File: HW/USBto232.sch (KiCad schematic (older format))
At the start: 14 parts

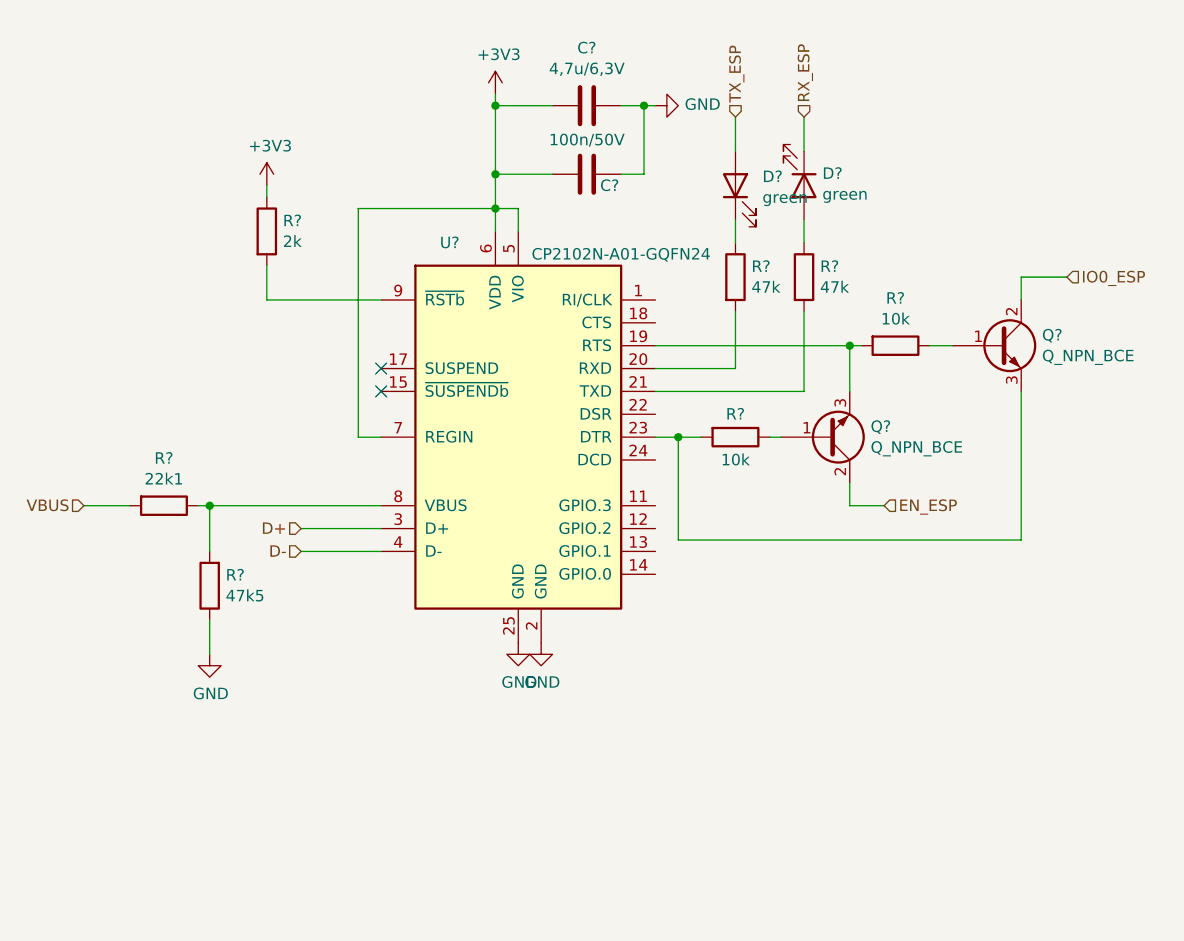
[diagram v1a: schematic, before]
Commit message: add some codes for JLCPCB, change package and schematic of CP2102
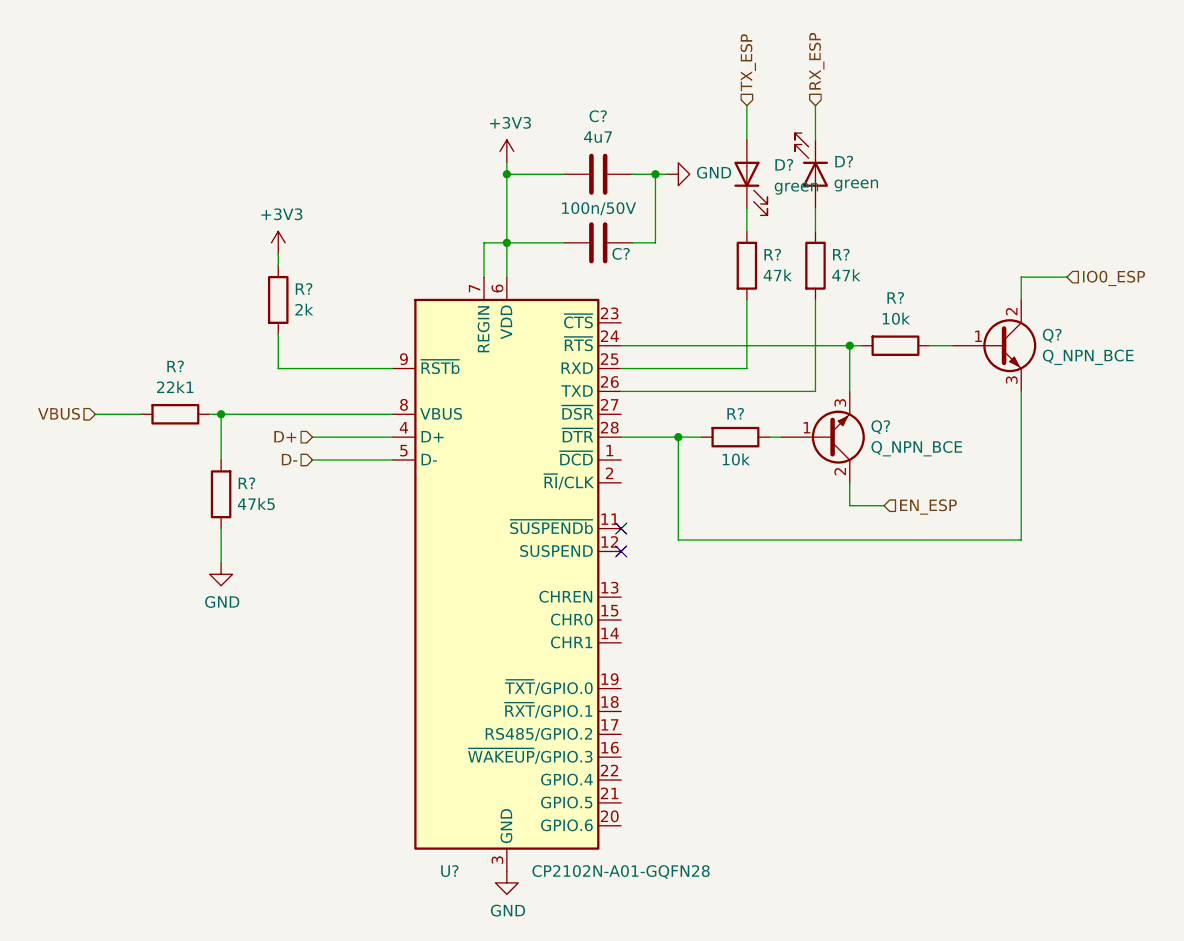
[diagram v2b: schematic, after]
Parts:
- removed U?: CP2102N-A01-GQFN24, Package_DFN_QFN:QFN-24-1EP_4x4mm_P0.5mm_EP2.6x2.6mm, symbol Interface_USB:CP2102N-A01-GQFN24
- added U?: CP2102N-A01-GQFN28, Package_DFN_QFN:QFN-28-1EP_5x5mm_P0.5mm_EP3.35x3.35mm, symbol Interface_USB:CP2102N-A01-GQFN28
- C?: value 4,7u/6,3V -> 4u7; LCSC (none) -> C23733
- R? (x2): LCSC (none) -> C25792
- R?: LCSC (none) -> C4109
- R? (x2): LCSC (none) -> C25744
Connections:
- net +3V3: now also U?.6 (VDD), U?.7 (REGIN)
- net D+: now also U?.4 (D+)
- net D-: now also U?.5 (D-)
- net GND: now also U?.29 (GND), U?.3 (GND)
- net at R?.2: now also U?.25 (RXD)
- net at R?.2: now also U?.26 (TXD)
- net at Q?.3 (E), R?.2: now also U?.24 (~RTS)
- net at Q?.3 (E), R?.2: now also U?.28 (~DTR)
- net at R?.1, R?.2: now also U?.8 (VBUS)
- net at R?.2: now also U?.9 (~RSTb)
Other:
- moved on the sheet: C?, D?, R?

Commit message: add some codes for JLCPCB
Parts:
- D? (x2): LCSC (none) -> C72043
- Q? (x2): LCSC (none) -> C20526
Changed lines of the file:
@@
 F 2 "Package_TO_SOT_SMD:SOT-23" H 7850 2800 50  0001 C CNN
 F 3 "~" H 7650 2700 50  0001 C CNN
+F 4 "C20526" H 7650 2700 50  0001 C CNN "LCSC"
 	1    7650 2700
 	1    0    0    -1
@@
 F 2 "Package_TO_SOT_SMD:SOT-23" H 7100 3200 50  0001 C CNN
 F 3 "~" H 6900 3100 50  0001 C CNN
+F 4 "C20526" H 6900 3100 50  0001 C CNN "LCSC"
 	1    6900 3100
 	1    0    0    1
@@
 F 2 "LED_SMD:LED_0603_1608Metric" H 6550 1950 50  0001 C CNN
 F 3 "~" H 6550 1950 50  0001 C CNN
+F 4 "C72043" H 6550 1950 50  0001 C CNN "LCSC"
 	1    6550 1950
 	0    -1   -1   0
@@
 F 2 "LED_SMD:LED_0603_1608Metric" H 6850 1950 50  0001 C CNN
 F 3 "~" H 6850 1950 50  0001 C CNN
+F 4 "C72043" H 6850 1950 50  0001 C CNN "LCSC"
 	1    6850 1950
 	0    1    1    0

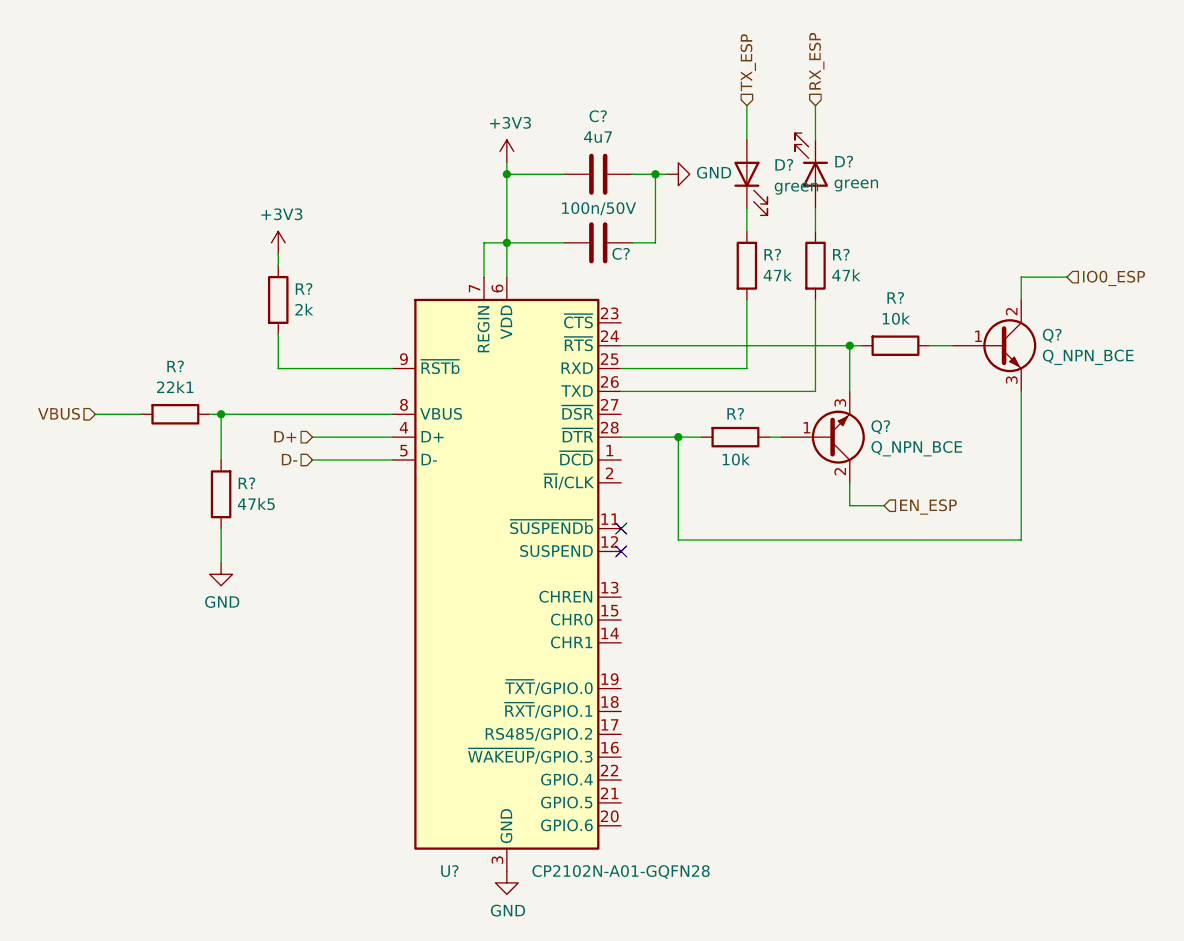
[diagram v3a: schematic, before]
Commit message: add footprint of inductor, add codes for JLCPCB, repair mistakes
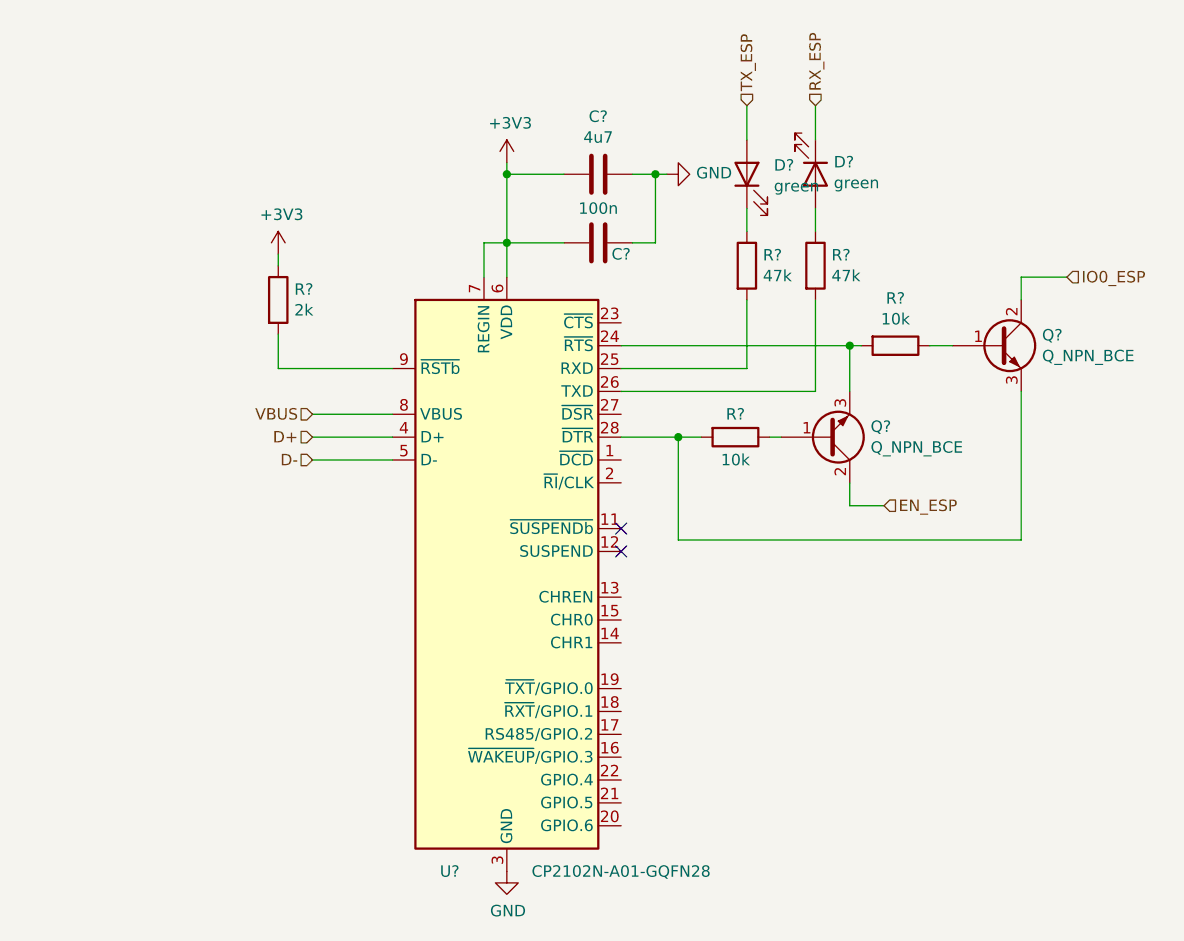
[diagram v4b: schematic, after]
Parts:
- removed R?: 22k1, Resistor_SMD:R_0402_1005Metric, symbol Device:R
- removed R?: 47k5, Resistor_SMD:R_0402_1005Metric, symbol Device:R
- C?: value 100n/50V -> 100n; LCSC (none) -> C1525
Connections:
- net VBUS: now also U?.8 (VBUS)
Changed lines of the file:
@@
 P 5900 2250
 F 0 "C?" V 5950 2350 50  0000 C CNN
-F 1 "100n/50V" V 5750 2250 50  0000 C CNN
+F 1 "100n" V 5750 2250 50  0000 C CNN
 F 2 "Capacitor_SMD:C_0402_1005Metric" H 5938 2100 50  0001 C CNN
 F 3 "~" H 5900 2250 50  0001 C CNN
+F 4 "C1525" H 5900 2250 50  0001 C CNN "LCSC"
 	1    5900 2250
 	0    1    1    0
@@
 	6200 1950 6150 1950
 Connection ~ 6150 1950
-$Comp
-L Device:R R?
-U 1 1 5FBDED92
-P 4050 3000
-F 0 "R?" V 3843 3000 50  0000 C CNN
-F 1 "22k1" V 3934 3000 50  0000 C CNN
-F 2 "Resistor_SMD:R_0402_1005Metric" V 3980 3000 50  0001 C CNN
-F 3 "~" H 4050 3000 50  0001 C CNN
-	1    4050 3000
-	0    1    1    0
-$EndComp
-$Comp
-L Device:R R?
-U 1 1 5FBDF92A
-P 4250 3350
-F 0 "R?" H 4180 3304 50  0000 R CNN
-F 1 "47k5" H 4180 3395 50  0000 R CNN
-F 2 "Resistor_SMD:R_0402_1005Metric" V 4180 3350 50  0001 C CNN
-F 3 "~" H 4250 3350 50  0001 C CNN
-	1    4250 3350
-	-1   0    0    1
-$EndComp
-Wire Wire Line
-	5000 3000 4250 3000
-Wire Wire Line
-	4250 3200 4250 3000
-Connection ~ 4250 3000
-Wire Wire Line
-	4250 3000 4200 3000
-$Comp
-L power:GND #PWR?
-U 1 1 5FBE16B9
-P 4250 3650
-F 0 "#PWR?" H 4250 3400 50  0001 C CNN
-F 1 "GND" H 4255 3477 50  0000 C CNN
-F 2 "" H 4250 3650 50  0001 C CNN
-F 3 "" H 4250 3650 50  0001 C CNN
-	1    4250 3650
-	1    0    0    -1
-$EndComp
-Wire Wire Line
-	4250 3500 4250 3650
 Wire Wire Line
 	4650 3100 5000 3100
@@
 Wire Wire Line
 	7000 3400 7150 3400
-Wire Wire Line
-	3700 3000 3900 3000
 $Comp
 L Device:R R?
@@
 Wire Wire Line
 	6850 2100 6850 2200
-Text HLabel 3700 3000 0    50   Input ~ 0
+Text HLabel 4650 3000 0    50   Input ~ 0
 VBUS
 Text HLabel 4650 3100 0    50   Input ~ 0
@@
 Wire Wire Line
 	6000 3100 6250 3100
+Wire Wire Line
+	4650 3000 5000 3000
 $EndSCHEMATC

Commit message: numbering components, place components on board
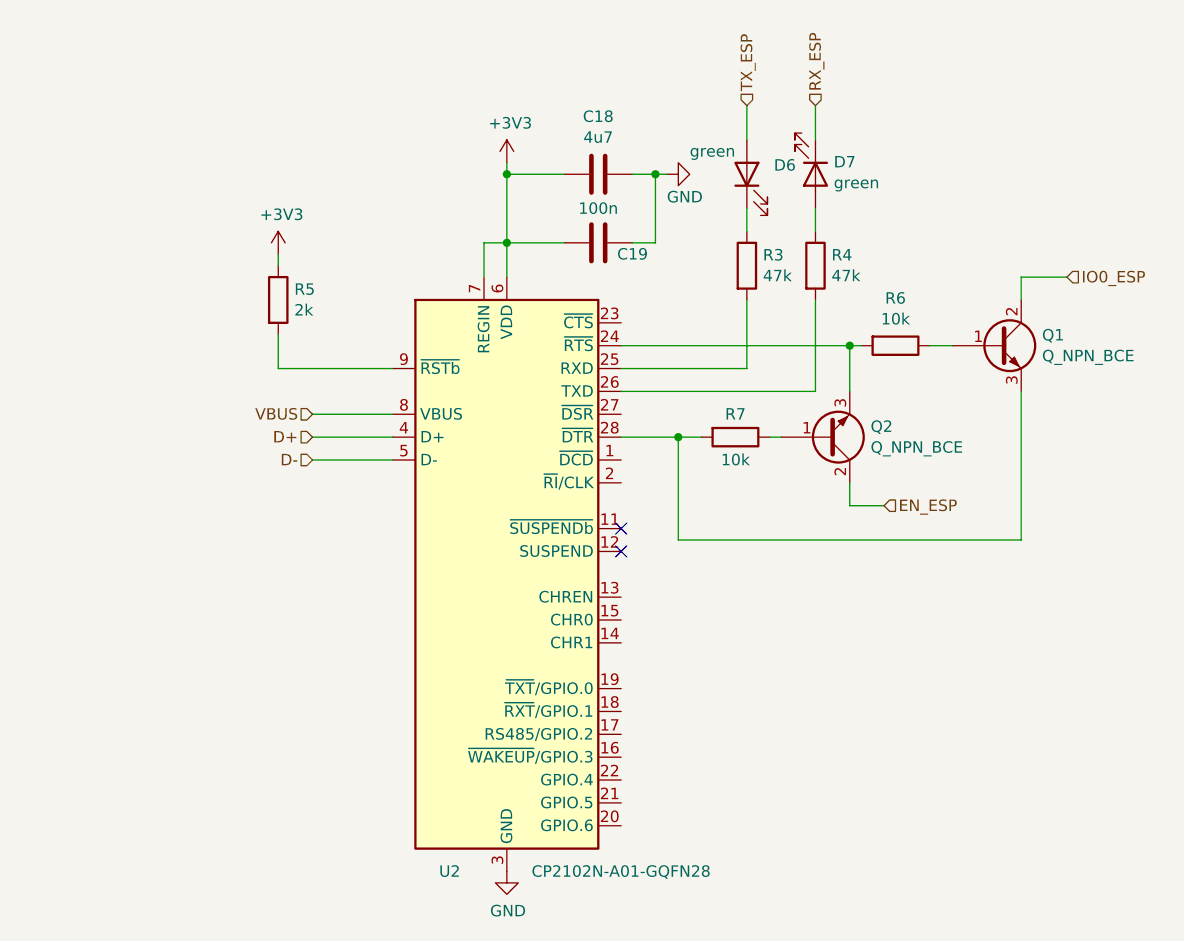
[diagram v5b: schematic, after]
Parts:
- gave numbers to parts that had none: 12
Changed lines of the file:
@@
 RX_ESP
 $Comp
-L power:GND #PWR?
+L power:GND #PWR0129
 U 1 1 5FBB9DA1
 P 5500 5000
-F 0 "#PWR?" H 5500 4750 50  0001 C CNN
+F 0 "#PWR0129" H 5500 4750 50  0001 C CNN
 F 1 "GND" H 5505 4827 50  0000 C CNN
 F 2 "" H 5500 5000 50  0001 C CNN
@@
 $EndComp
 $Comp
-L Device:R R?
+L Device:R R5
 U 1 1 5FBBF20B
 P 4500 2500
-F 0 "R?" H 4570 2546 50  0000 L CNN
+F 0 "R5" H 4570 2546 50  0000 L CNN
 F 1 "2k" H 4570 2455 50  0000 L CNN
 F 2 "Resistor_SMD:R_0402_1005Metric" V 4430 2500 50  0001 C CNN
@@
 	4500 2650 4500 2800
 $Comp
-L Device:R R?
+L Device:R R7
 U 1 1 5FBC264B
 P 6500 3100
-F 0 "R?" V 6400 3100 50  0000 C CNN
+F 0 "R7" V 6400 3100 50  0000 C CNN
 F 1 "10k" V 6600 3100 50  0000 C CNN
 F 2 "Resistor_SMD:R_0402_1005Metric" V 6430 3100 50  0001 C CNN
@@
 EN_ESP
 $Comp
-L Device:Q_NPN_BCE Q?
+L Device:Q_NPN_BCE Q1
 U 1 1 5FBC3B33
 P 7650 2700
-F 0 "Q?" H 7841 2746 50  0000 L CNN
+F 0 "Q1" H 7841 2746 50  0000 L CNN
 F 1 "Q_NPN_BCE" H 7841 2655 50  0000 L CNN
 F 2 "Package_TO_SOT_SMD:SOT-23" H 7850 2800 50  0001 C CNN
@@
 $EndComp
 $Comp
-L Device:R R?
+L Device:R R6
 U 1 1 5FBC5F56
 P 7200 2700
-F 0 "R?" V 6993 2700 50  0000 C CNN
+F 0 "R6" V 6993 2700 50  0000 C CNN
 F 1 "10k" V 7084 2700 50  0000 C CNN
 F 2 "Resistor_SMD:R_0402_1005Metric" V 7130 2700 50  0001 C CNN
@@
 	4500 2800 5000 2800
 $Comp
-L power:+3V3 #PWR?
+L power:+3V3 #PWR0130
 U 1 1 5FBD3E19
 P 4500 2300
-F 0 "#PWR?" H 4500 2150 50  0001 C CNN
+F 0 "#PWR0130" H 4500 2150 50  0001 C CNN
 F 1 "+3V3" H 4515 2473 50  0000 C CNN
 F 2 "" H 4500 2300 50  0001 C CNN
@@
 $EndComp
 $Comp
-L power:+3V3 #PWR?
+L power:+3V3 #PWR0131
 U 1 1 5FBD58C4
 P 5500 1900
-F 0 "#PWR?" H 5500 1750 50  0001 C CNN
+F 0 "#PWR0131" H 5500 1750 50  0001 C CNN
 F 1 "+3V3" H 5515 2073 50  0000 C CNN
 F 2 "" H 5500 1900 50  0001 C CNN
@@
 	5500 1900 5500 1950
 $Comp
-L Device:C C?
+L Device:C C18
 U 1 1 5FBD67B7
 P 5900 1950
-F 0 "C?" V 5648 1950 50  0000 C CNN
+F 0 "C18" V 5648 1950 50  0000 C CNN
 F 1 "4u7" V 5739 1950 50  0000 C CNN
 F 2 "Capacitor_SMD:C_1206_3216Metric" H 5938 1800 50  0001 C CNN
@@
 $EndComp
 $Comp
-L Device:C C?
+L Device:C C19
 U 1 1 5FBD6F93
 P 5900 2250
-F 0 "C?" V 5950 2350 50  0000 C CNN
+F 0 "C19" V 5950 2400 50  0000 C CNN
 F 1 "100n" V 5750 2250 50  0000 C CNN
 F 2 "Capacitor_SMD:C_0402_1005Metric" H 5938 2100 50  0001 C CNN
@@
 	6150 2250 6050 2250
 $Comp
-L power:GND #PWR?
+L power:GND #PWR0132
 U 1 1 5FBD8F58
 P 6200 1950
-F 0 "#PWR?" H 6200 1700 50  0001 C CNN
-F 1 "GND" V 6205 1822 50  0000 R CNN
+F 0 "#PWR0132" H 6200 1700 50  0001 C CNN
+F 1 "GND" V 6100 1950 50  0000 R CNN
 F 2 "" H 6200 1950 50  0001 C CNN
 F 3 "" H 6200 1950 50  0001 C CNN
@@
 	6650 3100 6700 3100
 $Comp
-L Device:Q_NPN_BCE Q?
+L Device:Q_NPN_BCE Q2
 U 1 1 5FBC010F
 P 6900 3100
-F 0 "Q?" H 7091 3054 50  0000 L CNN
+F 0 "Q2" H 7091 3054 50  0000 L CNN
 F 1 "Q_NPN_BCE" H 7091 3145 50  0000 L CNN
 F 2 "Package_TO_SOT_SMD:SOT-23" H 7100 3200 50  0001 C CNN
@@
 	7000 3400 7150 3400
 $Comp
-L Device:R R?
+L Device:R R3
 U 1 1 5F7740AD
 P 6550 2350
-F 0 "R?" H 6620 2396 50  0000 L CNN
+F 0 "R3" H 6620 2396 50  0000 L CNN
 F 1 "47k" H 6620 2305 50  0000 L CNN
 F 2 "Resistor_SMD:R_0402_1005Metric" V 6480 2350 50  0001 C CNN
@@
 $EndComp
 $Comp
-L Device:R R?
+L Device:R R4
 U 1 1 5F774323
 P 6850 2350
-F 0 "R?" H 6920 2396 50  0000 L CNN
+F 0 "R4" H 6920 2396 50  0000 L CNN
 F 1 "47k" H 6920 2305 50  0000 L CNN
 F 2 "Resistor_SMD:R_0402_1005Metric" V 6780 2350 50  0001 C CNN
@@
 $EndComp
 $Comp
-L Device:LED D?
+L Device:LED D6
 U 1 1 5F774688
 P 6550 1950
-F 0 "D?" V 6589 1832 50  0000 R CNN
-F 1 "green" V 6498 1832 50  0000 R CNN
+F 0 "D6" V 6589 1832 50  0000 R CNN
+F 1 "green" V 6650 2200 50  0000 R CNN
 F 2 "LED_SMD:LED_0603_1608Metric" H 6550 1950 50  0001 C CNN
 F 3 "~" H 6550 1950 50  0001 C CNN
@@
 $EndComp
 $Comp
-L Device:LED D?
+L Device:LED D7
 U 1 1 5F774C1B
 P 6850 1950
-F 0 "D?" V 6797 2030 50  0000 L CNN
+F 0 "D7" V 6797 2030 50  0000 L CNN
 F 1 "green" V 6888 2030 50  0000 L CNN
 F 2 "LED_SMD:LED_0603_1608Metric" H 6850 1950 50  0001 C CNN
@@
 D-
 $Comp
-L Interface_USB:CP2102N-A01-GQFN28 U?
+L Interface_USB:CP2102N-A01-GQFN28 U2
 U 1 1 5F8C3A3C
 P 5500 3700
-F 0 "U?" H 5250 2400 50  0000 C CNN
+F 0 "U2" H 5250 2400 50  0000 C CNN
 F 1 "CP2102N-A01-GQFN28" H 6000 2400 50  0000 C CNN
 F 2 "Package_DFN_QFN:QFN-28-1EP_5x5mm_P0.5mm_EP3.35x3.35mm" H 5950 2500 50  0001 L CNN

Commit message: ready for first prototype
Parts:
- C18: footprint Capacitor_SMD:C_1206_3216Metric -> Capacitor_SMD:C_0402_1005Metric
- D6, D7, Q1, Q2: JLCPCB_CORRECTION (none) -> 0;0;180
- U2: JLCPCB_CORRECTION (none) -> 0;0;270
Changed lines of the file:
@@
 F 3 "~" H 7650 2700 50  0001 C CNN
 F 4 "C20526" H 7650 2700 50  0001 C CNN "LCSC"
+F 5 "0;0;180" H 7650 2700 50  0001 C CNN "JLCPCB_CORRECTION"
 	1    7650 2700
 	1    0    0    -1
@@
 F 0 "C18" V 5648 1950 50  0000 C CNN
 F 1 "4u7" V 5739 1950 50  0000 C CNN
-F 2 "Capacitor_SMD:C_1206_3216Metric" H 5938 1800 50  0001 C CNN
+F 2 "Capacitor_SMD:C_0402_1005Metric" H 5938 1800 50  0001 C CNN
 F 3 "~" H 5900 1950 50  0001 C CNN
 F 4 "C23733" H 5900 1950 50  0001 C CNN "LCSC"
@@
 F 3 "~" H 6900 3100 50  0001 C CNN
 F 4 "C20526" H 6900 3100 50  0001 C CNN "LCSC"
+F 5 "0;0;180" H 6900 3100 50  0001 C CNN "JLCPCB_CORRECTION"
 	1    6900 3100
 	1    0    0    1
@@
 F 3 "~" H 6550 1950 50  0001 C CNN
 F 4 "C72043" H 6550 1950 50  0001 C CNN "LCSC"
+F 5 "0;0;180" H 6550 1950 50  0001 C CNN "JLCPCB_CORRECTION"
 	1    6550 1950
 	0    -1   -1   0
@@
 F 3 "~" H 6850 1950 50  0001 C CNN
 F 4 "C72043" H 6850 1950 50  0001 C CNN "LCSC"
+F 5 "0;0;180" H 6850 1950 50  0001 C CNN "JLCPCB_CORRECTION"
 	1    6850 1950
 	0    1    1    0
@@
 F 3 "https://www.silabs.com/documents/public/data-sheets/cp2102n-datasheet.pdf" H 5550 2950 50  0001 C CNN
 F 4 "C6568" H 5500 3700 50  0001 C CNN "LCSC"
+F 5 "0;0;270" H 5500 3700 50  0001 C CNN "JLCPCB_CORRECTION"
 	1    5500 3700
 	1    0    0    -1
